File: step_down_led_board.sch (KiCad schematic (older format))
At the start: 34 parts, among them CON1 BARREL_JACK, J1 OSHW Logo, J2 Polarity Mark, M1 BuckModule, M2 BuckModule, P1 CONN_02X20, P2 CONN_01X02, P3 CONN_01X05, P4 CONN_01X02, P5 CONN_01X02, P6 CONN_01X03, P9 CONN_01X06, Q1 Q_NMOS_GSD, Q2 Q_NMOS_GSD, Q3 Q_NMOS_GSD, Q4 Q_NMOS_GSD, Q5 Q_NMOS_GSD, Q9 Q_NMOS_GSD

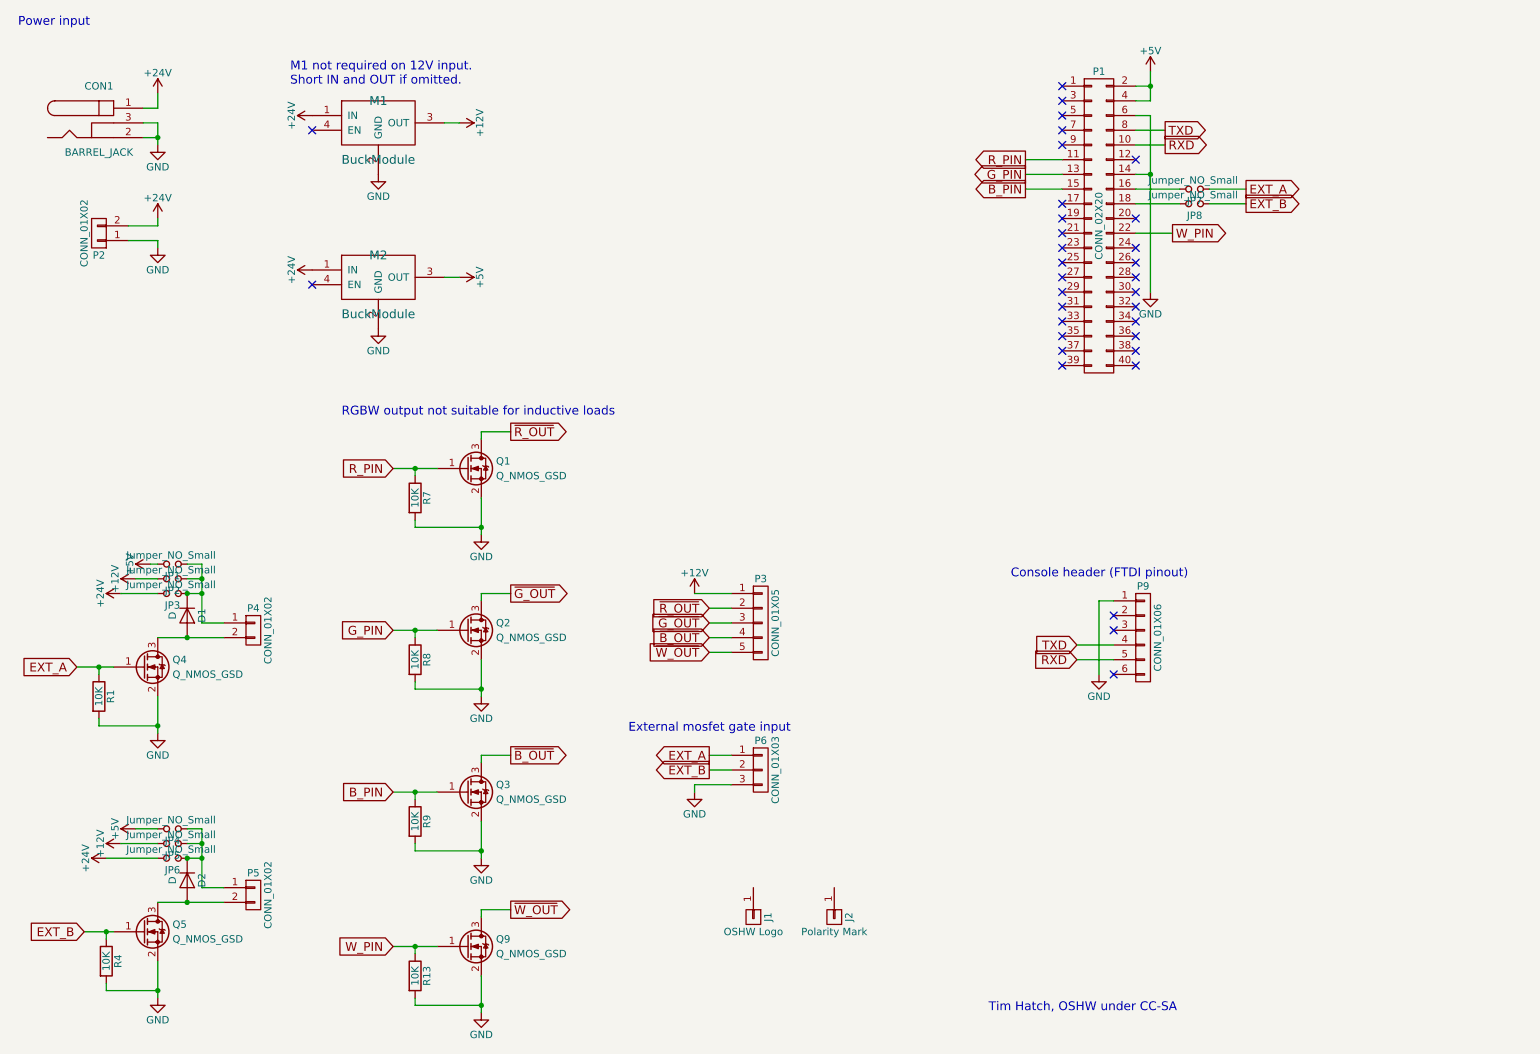
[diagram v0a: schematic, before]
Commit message: Include buck converter on board.
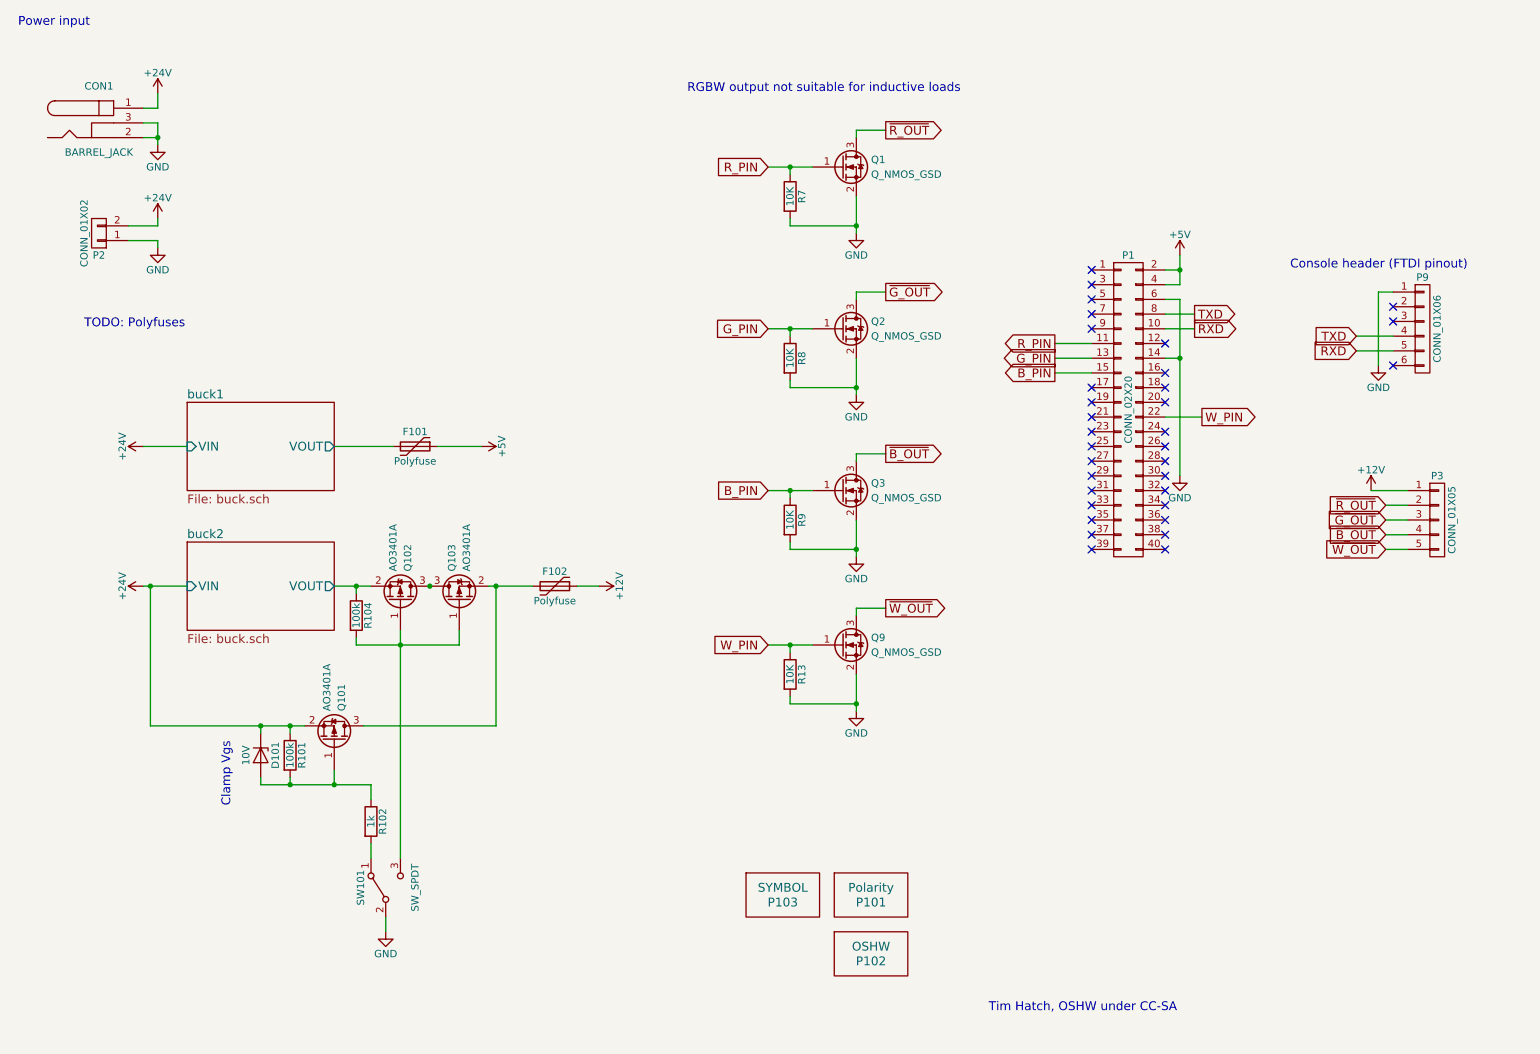
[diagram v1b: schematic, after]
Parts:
- removed D1, D2: D, Diodes_SMD:D_SOD-123, symbol D
- removed J1: OSHW Logo, Symbols:OSHW-Logo_11.4x12mm_SilkScreen, symbol CONN_01X01
- removed J2: Polarity Mark, Polarity:Polarity_Center_Positive_2mm_SilkScreen, symbol CONN_01X01
- removed JP1, JP2, JP3, JP4, JP5, JP6, JP7, JP8: Jumper_NO_Small, jumper:SOLDER-JUMPER_1-WAY, symbol Jumper_NO_Small
- removed M1, M2: BuckModule, BuckModule-Tim:BuckModule, symbol BuckModule
- removed P4, P5: CONN_01X02, Connectors_Molex:Molex_KK-6410-02_02x2.54mm_Straight, symbol CONN_01X02
- removed P6: CONN_01X03, Connectors_Molex:Molex_KK-6410-03_03x2.54mm_Straight, symbol CONN_01X03
- removed Q4, Q5: Q_NMOS_GSD, TO_SOT_Packages_SMD:SOT-23_Handsoldering, symbol Q_NMOS_GSD
- removed R1, R4: 10K, Resistors_SMD:R_0603, symbol R
- added D101: 10V, Diodes_SMD:D_SOD-123, symbol D_Zener
- added F101, F102: Polyfuse, Resistors_SMD:R_1210, symbol Polyfuse
- added P101: Polarity, Polarity_Symbols:Polarity_Center_Positive_2mm_SilkScreen, symbol SYMBOL
- added P102: OSHW, Symbols:OSHW-Logo_11.4x12mm_SilkScreen, symbol SYMBOL
- added P103: SYMBOL, Board_Outlines:Pi_Zero, symbol SYMBOL
- added Q101, Q102, Q103: AO3401A, TO_SOT_Packages_SMD:SOT-23, symbol Q_PMOS_GSD
- added R101, R104: 100k, Resistors_SMD:R_0603, symbol R
- added R102: 1k, Resistors_SMD:R_0603, symbol R
- added SW101: SW_SPDT, Buttons_Switches_SMD:SW_SPDT_PCM12, symbol SW_SPDT
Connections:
- net +12V: now also F102.1
- net +24V: now also D101.1 (K), Q101.2 (S), R101.1
- net +5V: now also F101.1
- net GND: now also SW101.2 (B)
- new net: Q102.1 (G), Q103.1 (G), R104.2, SW101.3 (C)
- new net: Q102.3 (D), Q103.3 (D)
- new net: D101.2 (A), Q101.1 (G), R101.2, R102.1
- new net: R102.2, SW101.1 (A)
- new net: F102.2, Q101.3 (D), Q103.2 (S)
- new net buck1/VOUT: F101.2
- new net buck2/VOUT: Q102.2 (S), R104.1
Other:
- note added: "Clamp Vgs"
- note added: "TODO: Polyfuses"
- note removed: "External mosfet gate input\n"
- note removed: "M1 not required on 12V input.\nShort IN and OUT if omitted."
- moved on the sheet: P1, P3, P9, Q1, Q2, Q3, Q9, R13, R7, R8, R9

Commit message: Massive changes, including makefile
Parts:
- added D2, D3: LED, LEDs:LED_0805, symbol LED
- added P6: US0001, OSHWA_Certification_Mark:OSHW_Mono_0.25_Scale, symbol SYMBOL
- added R4: 1k, Resistors_SMD:R_0603, symbol R
- added R5: 2k, Resistors_SMD:R_0603, symbol R
- F1: renamed from F101; footprint Resistors_SMD:R_1210 -> Resistors_SMD:R_1812
- F2: renamed from F102; footprint Resistors_SMD:R_1210 -> Resistors_SMD:R_1812
- renumbered D101 to D1, CON1 to P1, P103 to P3, P101 to P4, P102 to P5, P1 to P7, P9 to P8, P3 to P9, Q101 to Q1, Q103 to Q2, Q102 to Q3, Q1 to Q4, Q2 to Q5, Q3 to Q6, Q9 to Q7, R101 to R1, R102 to R2, R104 to R3, R7 to R6, R8 to R7, R9 to R8, R13 to R9, SW101 to SW1
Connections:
- net +12V: now also D3.2 (A)
- net +5V: now also D2.2 (A)
- net GND: now also R4.2, R5.2
- net buck2/VOUT: now also Q2.3 (D); no longer Q3.2 (S), R3.1
- net at Q3.3 (D): now also F2.2, Q1.3 (D); no longer Q2.3 (D)
- new net: Q2.2 (S), Q3.2 (S), R3.1
- new net: D2.1 (K), R4.1
- new net: D3.1 (K), R5.1
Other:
- note removed: "TODO: Polyfuses"
- moved on the sheet: F1, Q2, Q3, R3

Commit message: Update OSH Certification
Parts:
- P6: value US0001 -> US0118
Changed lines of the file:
@@
 P 6600 7500
 F 0 "P6" H 6600 7450 60  0000 C CNN
-F 1 "US0001" H 6600 7550 60  0000 C CNN
+F 1 "US0118" H 6600 7550 60  0000 C CNN
 F 2 "OSHWA_Certification_Mark:OSHW_Mono_0.25_Scale" H 6600 7500 60  0001 C CNN
 F 3 "" H 6600 7500 60  0001 C CNN
